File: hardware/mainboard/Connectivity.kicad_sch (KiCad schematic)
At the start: 25 parts, among them U2 FT230XS

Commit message: chore: sync
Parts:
- removed C34, C44: 100nF, Capacitor_SMD:C_0603_1608Metric, symbol Device:C_Small
- removed R71: 10k, Resistor_SMD:R_0603_1608Metric, symbol Device:R_Small
- removed U2: FT230XS, Package_SO:SSOP-16_3.9x4.9mm_P0.635mm, symbol Interface_USB:FT230XS
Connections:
- net FTDIU+ is gone; now on net FTDI_RX: R7.2
- net FTDIU- is gone; now on net FTDI_TX: R8.1
- net EX_D+ renamed EX_FTDI_D+
- net EX_D- renamed EX_FTDI_D-
- no-connect marks 9 -> 3
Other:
- moved on the sheet: C101, C102, C103, C104, C105, D11, D12, D25, D26, D4, R15, R17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

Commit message: chore: sync
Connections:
- net EX_CANFD1_RX: no longer D4.2 (K)
- net EX_CANFD1_TX: no longer D4.1 (K)
- net EX_CANFD2_RX: no longer D11.2 (K)
- net EX_CANFD2_TX: no longer D11.1 (K)
- net EX_FTDI_D+: no longer D12.1 (K)
- net EX_FTDI_D-: no longer D12.2 (K)
- net FTDI_RX: now also D12.1 (K)
- net FTDI_TX: now also D12.2 (K)
- net UC_CANFD1_RX: now also D4.2 (K)
- net UC_CANFD1_TX: now also D4.1 (K)
- net UC_CANFD2_RX: now also D11.2 (K)
- net UC_CANFD2_TX: now also D11.1 (K)
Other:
- moved on the sheet: D11, D12, D4, R15, R18, R19, R69, R7, R8

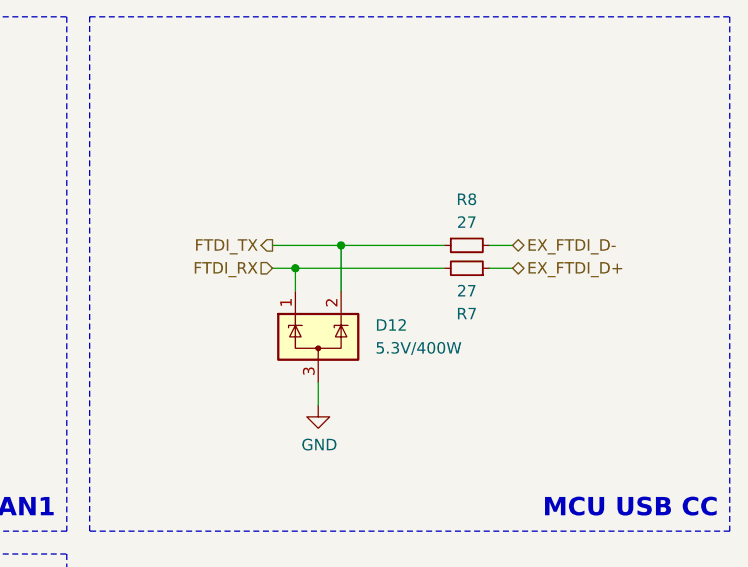
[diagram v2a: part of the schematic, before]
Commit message: Cleaned up schematic, changed USB to UART, changed pinout of AIR sandwich connector
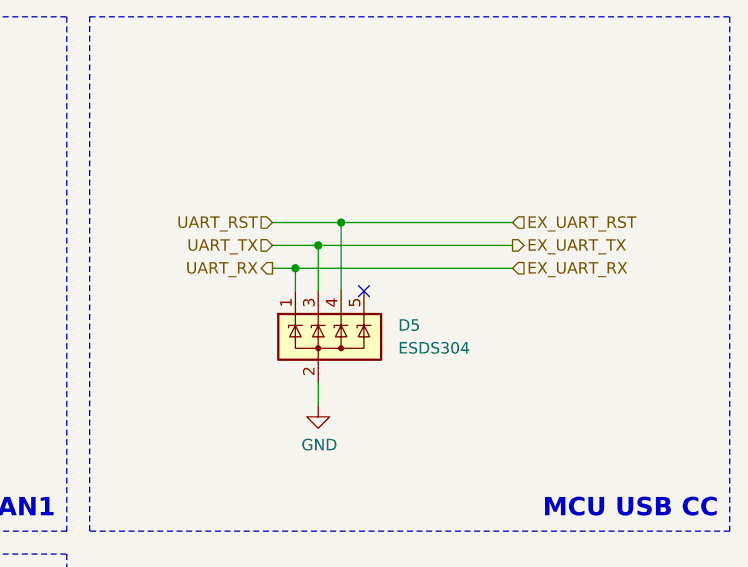
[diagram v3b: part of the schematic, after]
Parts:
- removed D12: 5.3V/400W, Package_TO_SOT_SMD:SOT-23-3, symbol Power_Protection:ESDA5V3L
- removed R7, R8: 27, Resistor_SMD:R_0603_1608Metric, symbol Device:R_Small
- added D5: ESDS304, Package_TO_SOT_SMD:SOT-23-5_HandSoldering, symbol Power_Protection:ESDS304
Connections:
- net GND: now also D5.2 (A)
- new net EX_UART_RST: D5.4 (K)
- new net EX_UART_RX: D5.1 (K)
- new net EX_UART_TX: D5.3 (K)
- no-connect marks 3 -> 4

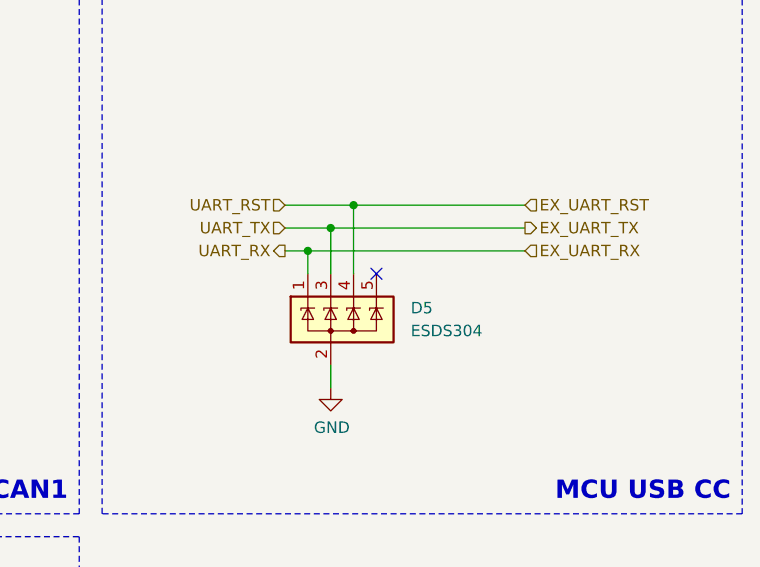
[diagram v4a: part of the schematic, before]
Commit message: Plytka chyba fajnie zrobiona oprocz teardropow bo kicad 10 jest dziwny
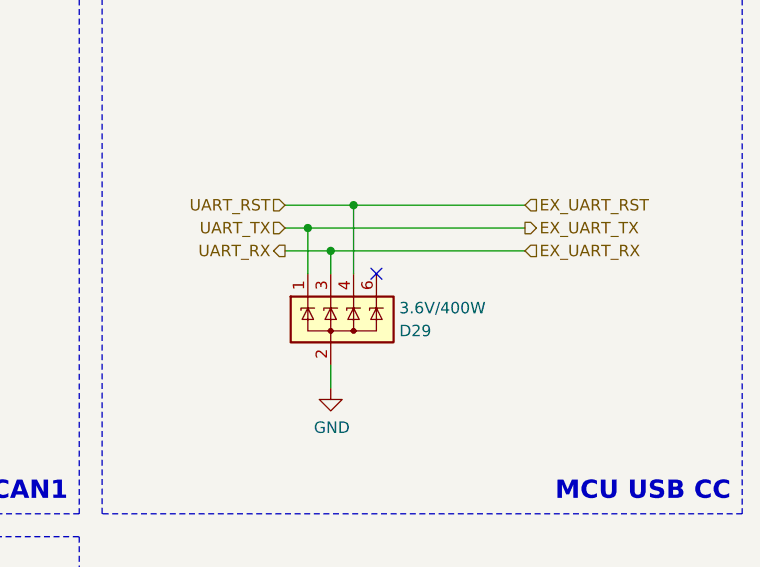
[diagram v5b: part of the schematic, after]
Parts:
- removed D5: ESDS304, Package_TO_SOT_SMD:SOT-23-5_HandSoldering, symbol Power_Protection:ESDS304
- added D29: 3.6V/400W, Package_TO_SOT_SMD:SOT-23-6, symbol Power_Protection:ESDA5V3SC5
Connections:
- net EX_UART_RST: now also D29.4 (A)
- net EX_UART_RX: now also D29.3 (A)
- net EX_UART_TX: now also D29.1 (A)
- net GND: now also D29.2 (K), D29.5 (NC)
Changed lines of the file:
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@@
 	)
 	(junction
-		(at 149.86 100.33)
+		(at 303.53 85.09)
 		(diameter 0)
 		(color 0 0 0 0)
 	)
 	(junction
-		(at 238.76 144.78)
+		(at 306.07 87.63)
 		(diameter 0)
 		(color 0 0 0 0)
 	)
 	(junction
-		(at 116.84 143.51)
+		(at 149.86 100.33)
+		(diameter 0)
+		(color 0 0 0 0)
+	)
+	(junction
+		(at 238.76 144.78)
 		(diameter 0)
 		(color 0 0 0 0)
 	)
 	(junction
-		(at 306.07 85.09)
+		(at 116.84 143.51)
 		(diameter 0)
 		(color 0 0 0 0)
@@
 		(color 0 0 0 0)
 	)
-	(junction
-		(at 303.53 87.63)
-		(diameter 0)
-		(color 0 0 0 0)
-	)
 	(no_connect
 		(at 124.46 204.47)
@@
 	(wire
 		(pts
-			(xy 306.07 85.09) (xy 327.66 85.09)
+			(xy 149.86 201.93) (xy 149.86 204.47)
 		)
 		(stroke
@@
 	(wire
 		(pts
-			(xy 149.86 201.93) (xy 149.86 204.47)
+			(xy 300.99 82.55) (xy 308.61 82.55)
 		)
 		(stroke
@@
 	(wire
 		(pts
-			(xy 300.99 82.55) (xy 308.61 82.55)
+			(xy 300.99 87.63) (xy 306.07 87.63)
 		)
 		(stroke
@@
 	(wire
 		(pts
-			(xy 300.99 87.63) (xy 303.53 87.63)
+			(xy 238.76 86.36) (xy 246.38 86.36)
 		)
 		(stroke
@@
 	(wire
 		(pts
-			(xy 238.76 86.36) (xy 246.38 86.36)
+			(xy 149.86 73.66) (xy 149.86 76.2)
 		)
 		(stroke
@@
 	(wire
 		(pts
-			(xy 149.86 73.66) (xy 149.86 76.2)
+			(xy 303.53 85.09) (xy 303.53 90.17)
 		)
 		(stroke
@@
 	(wire
 		(pts
+			(xy 303.53 85.09) (xy 327.66 85.09)
+		)
+		(stroke
+			(width 0)
+			(type default)
+		)
+	)
+	(wire
+		(pts
 			(xy 251.46 142.24) (xy 254 142.24)
 		)
@@
 	(wire
 		(pts
-			(xy 157.48 100.33) (xy 160.02 100.33)
+			(xy 306.07 87.63) (xy 327.66 87.63)
 		)
 		(stroke
@@
 	(wire
 		(pts
-			(xy 116.84 73.66) (xy 116.84 102.87)
+			(xy 157.48 100.33) (xy 160.02 100.33)
 		)
 		(stroke
@@
 	(wire
 		(pts
-			(xy 303.53 87.63) (xy 303.53 90.17)
+			(xy 116.84 73.66) (xy 116.84 102.87)
 		)
 		(stroke
@@
 	(wire
 		(pts
-			(xy 238.76 144.78) (xy 238.76 147.32)
+			(xy 306.07 87.63) (xy 306.07 90.17)
 		)
 		(stroke
@@
 	(wire
 		(pts
-			(xy 306.07 85.09) (xy 306.07 90.17)
+			(xy 238.76 144.78) (xy 238.76 147.32)
 		)
 		(stroke
@@
 	(wire
 		(pts
-			(xy 303.53 87.63) (xy 327.66 87.63)
-		)
-		(stroke
-			(width 0)
-			(type default)
-		)
-	)
-	(wire
-		(pts
 			(xy 116.84 143.51) (xy 116.84 204.47)
 		)
@@
 	(wire
 		(pts
-			(xy 300.99 85.09) (xy 306.07 85.09)
+			(xy 300.99 85.09) (xy 303.53 85.09)
 		)
 		(stroke
@@
 	)
 	(symbol
-		(lib_id "Power_Protection:ESDS304")
-		(at 306.07 95.25 0)
-		(unit 1)
-		(body_style 1)
-		(exclude_from_sim no)
-		(in_bom yes)
-		(on_board yes)
-		(in_pos_files yes)
-		(dnp no)
-		(fields_autoplaced yes)
-		(property "Reference" "D5"
-			(at 314.96 93.9799 0)
-			(show_name no)
-			(do_not_autoplace no)
-			(effects
-				(font
-					(size 1.27 1.27)
-				)
-				(justify left)
-			)
-		)
-		(property "Value" "ESDS304"
-			(at 314.96 96.5199 0)
-			(show_name no)
-			(do_not_autoplace no)
-			(effects
-				(font
-					(size 1.27 1.27)
-				)
-				(justify left)
-			)
-		)
-		(property "Footprint" "Package_TO_SOT_SMD:SOT-23-5_HandSoldering"
-			(at 292.1 113.03 0)
-			(hide yes)
-			(show_name no)
-			(do_not_autoplace no)
-			(effects
-				(font
-					(size 1.27 1.27)
-				)
-				(justify left)
-			)
-		)
-		(property "Datasheet" "https://www.ti.com/lit/ds/symlink/esds304.pdf"
-			(at 306.07 107.95 0)
-			(hide yes)
-			(show_name no)
-			(do_not_autoplace no)
-			(effects
-				(font
-					(size 1.27 1.27)
-				)
-			)
-		)
-		(property "Description" "4-channel 1Gbps TVS Diode Array, 2.3pF, 4.5V breakdown, 30kV contact & air gap, SOT-23-5"
-			(at 307.34 110.49 0)
-			(hide yes)
-			(show_name no)
-			(do_not_autoplace no)
-			(effects
-				(font
-					(size 1.27 1.27)
-				)
-			)
-		)
-		(property "Mouser Part Number" " 595-ESDS304DBVR "
-			(at 306.07 95.25 0)
-			(hide yes)
-			(show_name no)
-			(do_not_autoplace no)
-			(effects
-				(font
-					(size 1.27 1.27)
-				)
-			)
-		)
-		(pin "2"
-		)
-		(pin "5"
-		)
-		(pin "4"
-		)
-		(pin "1"
-		)
-		(pin "3"
-		)
-		(instances
-			(project "PUTM_EV_AMS_MASTER"
-				(path "/b456cffc-d9d7-4c91-91f2-36ec9a65dd1b/c7d64097-44d3-49d9-9a80-8f2f4ff55e04"
-					(reference "D5")
-					(unit 1)
-				)
-			)
-		)
-	)
-	(symbol
 		(lib_name "ESDA5V3SC5_3")
 		(lib_id "Power_Protection:ESDA5V3SC5")
@@
 					(unit 1)
 				)
+			)
+		)
+	)
+	(symbol
+		(lib_name "ESDA5V3SC5_3")
+		(lib_id "Power_Protection:ESDA5V3SC5")
+		(at 306.07 95.25 0)
+		(unit 1)
+		(body_style 1)
+		(exclude_from_sim no)
+		(in_bom yes)
+		(on_board yes)
+		(in_pos_files yes)
+		(dnp no)
+		(property "Reference" "D29"
+			(at 313.69 96.52 0)
+			(show_name no)
+			(do_not_autoplace no)
+			(effects
+				(font
+					(size 1.27 1.27)
+				)
+				(justify left)
+			)
+		)
+		(property "Value" "3.6V/400W"
+			(at 313.69 93.98 0)
+			(show_name no)
+			(do_not_autoplace no)
+			(effects
+				(font
+					(size 1.27 1.27)
+				)
+				(justify left)
+			)
+		)
+		(property "Footprint" "Package_TO_SOT_SMD:SOT-23-6"
+			(at 313.69 96.52 0)
+			(hide yes)
+			(show_name no)
+			(do_not_autoplace no)
+			(effects
+				(font
+					(size 1.27 1.27)
+				)
+				(justify left)
+			)
+		)
+		(property "Datasheet" "www.ti.com/lit/gpn/esds302"
+			(at 309.245 92.075 0)
+			(hide yes)
+			(show_name no)
+			(do_not_autoplace no)
+			(effects
+				(font
+					(size 1.27 1.27)
+				)
+			)
+		)
+		(property "Description" "ESD Protection Diodes / TVS Diodes Quad 2.3-pF 3.6-V +/-30-kV ESD protect"
+			(at 306.07 95.25 0)
+			(hide yes)
+			(show_name no)
+			(do_not_autoplace no)
+			(effects
+				(font
+					(size 1.27 1.27)
+				)
+			)
+		)
+		(property "Manufacturer_Part_Number" "ESDS304DBVR"
+			(at 306.07 95.25 0)
+			(hide yes)
+			(show_name no)
+			(do_not_autoplace no)
+			(effects
+				(font
+					(size 1.27 1.27)
+				)
+			)
+		)
+		(property "Mouser Part Number" "595-ESDS304DBVR"
+			(at 306.07 95.25 0)
+			(hide yes)
+			(show_name no)
+			(do_not_autoplace no)
+			(effects
+				(font
+					(size 1.27 1.27)
+				)
+			)
+		)
+		(property "Mouser Price/Stock" ""
+			(at 306.07 95.25 0)
+			(hide yes)
+			(show_name no)
+			(do_not_autoplace no)
+			(effects
+				(font
+					(size 1.27 1.27)
+				)
+			)
+		)
+		(property "Arrow Part Number" ""
+			(at 306.07 95.25 0)
+			(hide yes)
+			(show_name no)
+			(do_not_autoplace no)
+			(effects
+				(font
+					(size 1.27 1.27)
+				)
+			)
+		)
+		(property "Arrow Price/Stock" ""
+			(at 306.07 95.25 0)
+			(hide yes)
+			(show_name no)
+			(do_not_autoplace no)
+			(effects
+				(font
+					(size 1.27 1.27)
+				)
+			)
+		)
+		(property "DigiKey Part Number" ""
+			(at 306.07 95.25 0)
+			(show_name no)
+			(do_not_autoplace no)
+			(effects
+				(font
+					(size 1.27 1.27)
+				)
+			)
+		)
+		(pin "2"
+		)
+		(pin "3"
+		)
+		(pin "1"
+		)
+		(pin "4"
+		)
+		(pin "5"
+		)
+		(pin "6"
+		)
+		(instances
+			(project "PUTM_EV_AMS_MASTER"
+				(path "/b456cffc-d9d7-4c91-91f2-36ec9a65dd1b/c7d64097-44d3-49d9-9a80-8f2f4ff55e04"
+					(reference "D29")
+					(unit 1)
+				)

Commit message: sync
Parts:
- removed C101, C102, C103, C104, C105: 10nF, Capacitor_SMD:C_0603_1608Metric, symbol Device:C_Small
- removed D11, D4: 5.3V/400W, Package_TO_SOT_SMD:SOT-23-3, symbol Power_Protection:ESDA5V3L
- removed R15, R17, R18, R19, R20, R21, R25, R26, R69: 27, Resistor_SMD:R_0603_1608Metric, symbol Device:R_Small
- added D31: 3.6V/400W, Package_TO_SOT_SMD:SOT-23-6, symbol Power_Protection:ESDA5V3SC5
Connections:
- net UC_AIR_AUX_M is gone; now on net EX_AIR_AUX_M: D25.3 (A)
- net UC_AIR_AUX_P is gone; now on net EX_AIR_AUX_P: D25.4 (A)
- net UC_AIR_AUX_PRE is gone; now on net EX_AIR_AUX_PRE: D25.1 (A)
- net UC_IN1 is gone; now on net EX_IN1: D26.1 (A)
- net UC_IN2 is gone; now on net EX_IN2: D26.3 (A)
- net GND: now also D31.2 (K), D31.5 (NC)
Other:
- note removed: "CAN2"
- moved on the sheet: D25, D26
